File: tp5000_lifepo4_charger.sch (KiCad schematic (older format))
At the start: 23 parts, among them J1 VIN, J2 GND, J3 VOUT, J4 GND, J5 BAT+, J6 BAT-, P1 USB_C_Plug_USB2.0, U1 TP5000, U2 DW01, U3 FS8205A

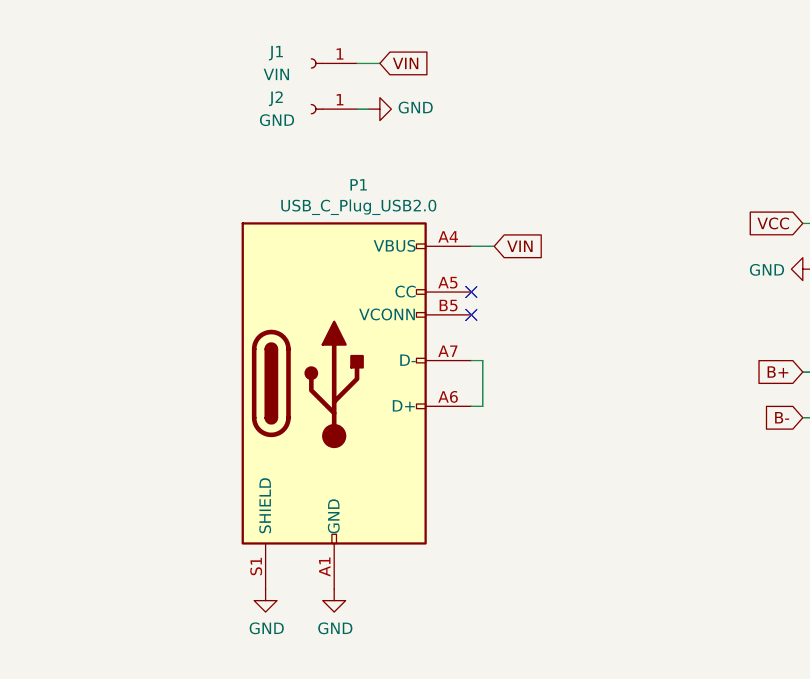
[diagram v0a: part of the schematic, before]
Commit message: changed footprint solder connection in schematic
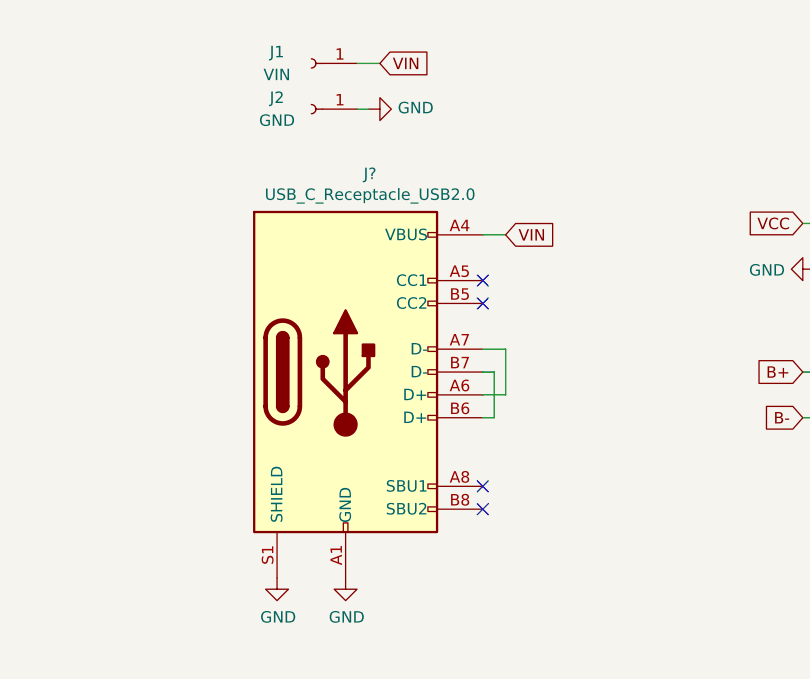
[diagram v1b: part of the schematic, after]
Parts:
- removed P1: USB_C_Plug_USB2.0, Connector_USB:USB_C_Receptacle_HRO_TYPE-C-31-M-12, symbol Connector:USB_C_Plug_USB2.0
- added J?: USB_C_Receptacle_USB2.0, symbol Connector:USB_C_Receptacle_USB2.0
- J1, J2, J3, J4, J5, J6: footprint TestPoint:TestPoint_THTPad_4.0x4.0mm_Drill2.0mm -> TestPoint:TestPoint_THTPad_2.5x2.5mm_Drill1.2mm
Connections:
- net GND: now also J?.A1 (GND), J?.A12 (GND), J?.B1 (GND), J?.B12 (GND), J?.S1 (SHIELD)
- net VIN: now also J?.A4 (VBUS), J?.A9 (VBUS), J?.B4 (VBUS), J?.B9 (VBUS)
- new net: J?.A6 (D+), J?.A7 (D-)
- new net: J?.B6 (D+), J?.B7 (D-)
- no-connect marks 6 -> 8
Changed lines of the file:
@@
-$EndComp
-$Comp
-L Connector:USB_C_Plug_USB2.0 P1
-U 1 1 638CC637
-P 2550 6550
-F 0 "P1" H 2657 7417 50  0000 C CNN
-F 1 "USB_C_Plug_USB2.0" H 2657 7326 50  0000 C CNN
-F 2 "Connector_USB:USB_C_Receptacle_HRO_TYPE-C-31-M-12" H 2700 6550 50  0001 C CNN
-F 3 "https://www.lcsc.com/product-detail/span-style-background-color-ff0-USB-span-Connectors_Korean-Hroparts-Elec-TYPE-C-31-M-12_C165948.html" H 2700 6550 50  0001 C CNN
-	1    2550 6550
-	1    0    0    -1
 $EndComp
 $Comp
@@
 F 0 "J2" H 2600 5300 50  0000 C CNN
 F 1 "GND" H 2600 5400 50  0000 C CNN
-F 2 "TestPoint:TestPoint_THTPad_4.0x4.0mm_Drill2.0mm" H 2450 5350 50  0001 C CNN
+F 2 "TestPoint:TestPoint_THTPad_2.5x2.5mm_Drill1.2mm" H 2450 5350 50  0001 C CNN
 F 3 "~" H 2450 5350 50  0001 C CNN
 	1    2450 5350
@@
 F 0 "J1" H 2600 5100 50  0000 C CNN
 F 1 "VIN" H 2600 5200 50  0000 C CNN
-F 2 "TestPoint:TestPoint_THTPad_4.0x4.0mm_Drill2.0mm" H 2450 5150 50  0001 C CNN
+F 2 "TestPoint:TestPoint_THTPad_2.5x2.5mm_Drill1.2mm" H 2450 5150 50  0001 C CNN
 F 3 "~" H 2450 5150 50  0001 C CNN
 	1    2450 5150
@@
 F 0 "J3" H 4928 5876 50  0000 L CNN
 F 1 "VOUT" H 4928 5785 50  0000 L CNN
-F 2 "TestPoint:TestPoint_THTPad_4.0x4.0mm_Drill2.0mm" H 4900 5850 50  0001 C CNN
+F 2 "TestPoint:TestPoint_THTPad_2.5x2.5mm_Drill1.2mm" H 4900 5850 50  0001 C CNN
 F 3 "~" H 4900 5850 50  0001 C CNN
 	1    4900 5850
@@
 F 0 "J5" H 4928 6526 50  0000 L CNN
 F 1 "BAT+" H 4928 6435 50  0000 L CNN
-F 2 "TestPoint:TestPoint_THTPad_4.0x4.0mm_Drill2.0mm" H 4900 6500 50  0001 C CNN
+F 2 "TestPoint:TestPoint_THTPad_2.5x2.5mm_Drill1.2mm" H 4900 6500 50  0001 C CNN
 F 3 "~" H 4900 6500 50  0001 C CNN
 	1    4900 6500
@@
 F 0 "J6" H 4928 6726 50  0000 L CNN
 F 1 "BAT-" H 4928 6635 50  0000 L CNN
-F 2 "TestPoint:TestPoint_THTPad_4.0x4.0mm_Drill2.0mm" H 4900 6700 50  0001 C CNN
+F 2 "TestPoint:TestPoint_THTPad_2.5x2.5mm_Drill1.2mm" H 4900 6700 50  0001 C CNN
 F 3 "~" H 4900 6700 50  0001 C CNN
 	1    4900 6700
@@
 L power:GND #PWR06
 U 1 1 638F36E3
-P 2550 7450
-F 0 "#PWR06" H 2550 7200 50  0001 C CNN
-F 1 "GND" H 2555 7277 50  0000 C CNN
-F 2 "" H 2550 7450 50  0001 C CNN
-F 3 "" H 2550 7450 50  0001 C CNN
-	1    2550 7450
+P 2600 7400
+F 0 "#PWR06" H 2600 7150 50  0001 C CNN
+F 1 "GND" H 2605 7227 50  0000 C CNN
+F 2 "" H 2600 7400 50  0001 C CNN
+F 3 "" H 2600 7400 50  0001 C CNN
+	1    2600 7400
 	1    0    0    -1
 $EndComp
@@
 Wire Wire Line
 	3350 1850 3350 1900
-Text GLabel 3250 5950 2    50   Input ~ 0
+Text GLabel 3300 5900 2    50   Input ~ 0
 VIN
-Wire Wire Line
-	3150 5950 3250 5950
-Wire Wire Line
-	3150 6450 3200 6450
-Wire Wire Line
-	3200 6450 3200 6650
-Wire Wire Line
-	3200 6650 3150 6650
-NoConn ~ 3150 6150
-NoConn ~ 3150 6250
 Text GLabel 4600 6500 0    50   Input ~ 0
 B+
@@
 F 0 "J4" H 4928 6076 50  0000 L CNN
 F 1 "GND" H 4928 5985 50  0000 L CNN
-F 2 "TestPoint:TestPoint_THTPad_4.0x4.0mm_Drill2.0mm" H 4900 6050 50  0001 C CNN
+F 2 "TestPoint:TestPoint_THTPad_2.5x2.5mm_Drill1.2mm" H 4900 6050 50  0001 C CNN
 F 3 "~" H 4900 6050 50  0001 C CNN
 	1    4900 6050
@@
 L power:GND #PWR04
 U 1 1 63971526
-P 2250 7450
-F 0 "#PWR04" H 2250 7200 50  0001 C CNN
-F 1 "GND" H 2255 7277 50  0000 C CNN
-F 2 "" H 2250 7450 50  0001 C CNN
-F 3 "" H 2250 7450 50  0001 C CNN
-	1    2250 7450
+P 2300 7400
+F 0 "#PWR04" H 2300 7150 50  0001 C CNN
+F 1 "GND" H 2305 7227 50  0000 C CNN
+F 2 "" H 2300 7400 50  0001 C CNN
+F 3 "" H 2300 7400 50  0001 C CNN
+	1    2300 7400
 	1    0    0    -1
 $EndComp
@@
 Text GLabel 1750 3750 3    50   Input ~ 0
 VIN
+$Comp
+L Connector:USB_C_Receptacle_USB2.0 J?
+U 1 1 640C46BA
+P 2600 6500
+F 0 "J?" H 2707 7367 50  0000 C CNN
+F 1 "USB_C_Receptacle_USB2.0" H 2707 7276 50  0000 C CNN
+F 2 "" H 2750 6500 50  0001 C CNN
+F 3 "https://www.usb.org/sites/default/files/documents/usb_type-c.zip" H 2750 6500 50  0001 C CNN
+	1    2600 6500
+	1    0    0    -1
+$EndComp
+Wire Wire Line
+	3200 5900 3300 5900
+Wire Wire Line
+	3200 6400 3300 6400
+Wire Wire Line
+	3300 6400 3300 6600
+Wire Wire Line
+	3300 6600 3200 6600
+Wire Wire Line
+	3200 6500 3250 6500
+Wire Wire Line
+	3250 6500 3250 6700
+Wire Wire Line
+	3250 6700 3200 6700
+NoConn ~ 3200 6100
+NoConn ~ 3200 6200
+NoConn ~ 3200 7000
+NoConn ~ 3200 7100
 $EndSCHEMATC
